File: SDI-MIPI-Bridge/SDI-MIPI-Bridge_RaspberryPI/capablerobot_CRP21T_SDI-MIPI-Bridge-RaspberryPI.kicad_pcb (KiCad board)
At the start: 2 copper layers, 25.5 x 99.8 mm, 2 parts, among them J1 WE_686715100001_FLEX, J2 WE_687650100002_FLEX

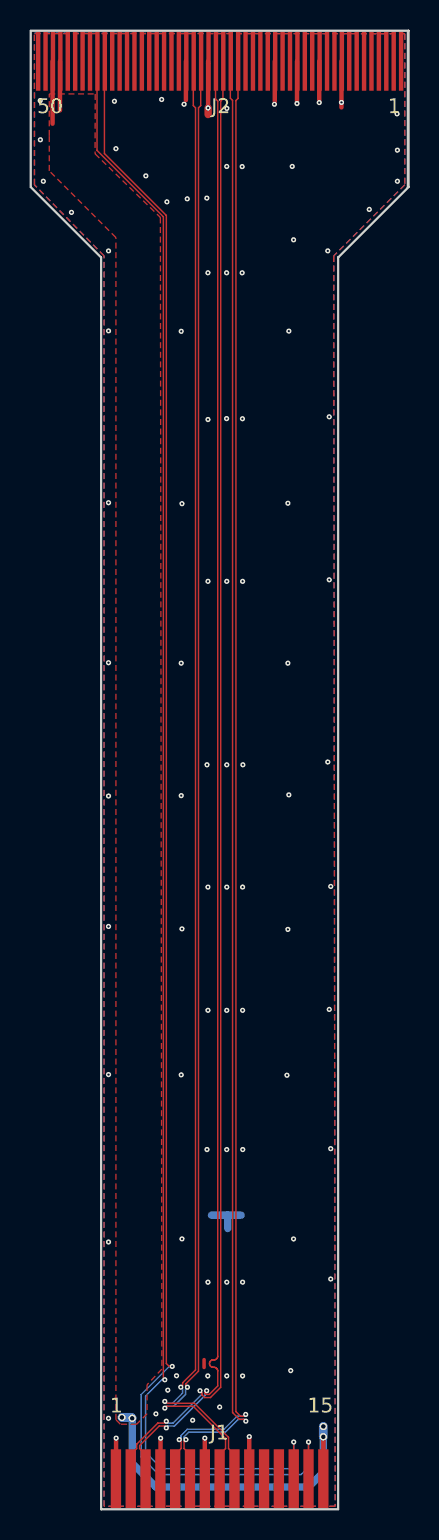
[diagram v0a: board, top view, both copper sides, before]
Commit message: Sync nets to double up I2C pins and add RST / IO connection
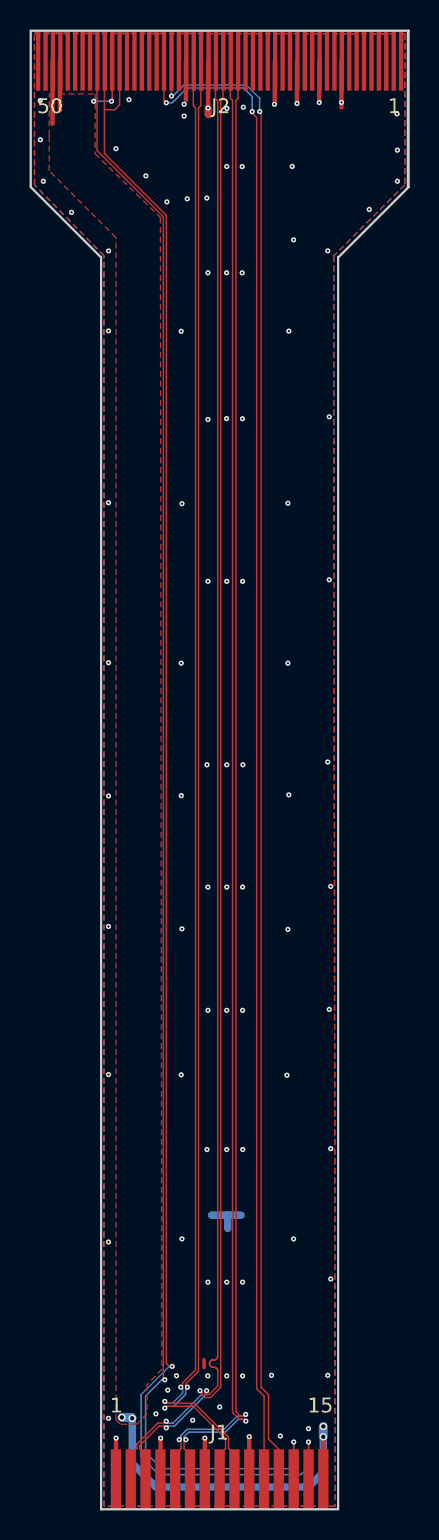
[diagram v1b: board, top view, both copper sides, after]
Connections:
- J1 pad 11: /EN -> /RST
- J2 pad 32: /VSYNC -> /IO1
- J2 pad 33: Net-(J2-Pad33) -> /RST
- J2 pad 39: Net-(J2-Pad39) -> /SDA
- J2 pad 40: Net-(J2-Pad40) -> /SCL
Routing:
- net /RST: track 0.00 -> 103.0 mm, vias 0 -> 2
- net /IO1: track 0.00 -> 102.7 mm, vias 0 -> 2
- net /SCL: track 111.0 -> 115.2 mm, vias 2 -> 4
- net /SDA: track 113.4 -> 117.5 mm
- net /GND: vias 94 -> 98
